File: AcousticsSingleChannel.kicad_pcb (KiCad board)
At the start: 4 copper layers, 25.4 x 25.4 mm, 51 parts, among them J1 Conn_01x04_Pin, J2 Conn_01x04_Pin, J4 Conn_01x09_Pin, U1 OPA1604AIPWR, U2 OPA1604AIPWR, U3 LTC6910-3CTS8#TRPBF, U4 ADS7042IDCUR

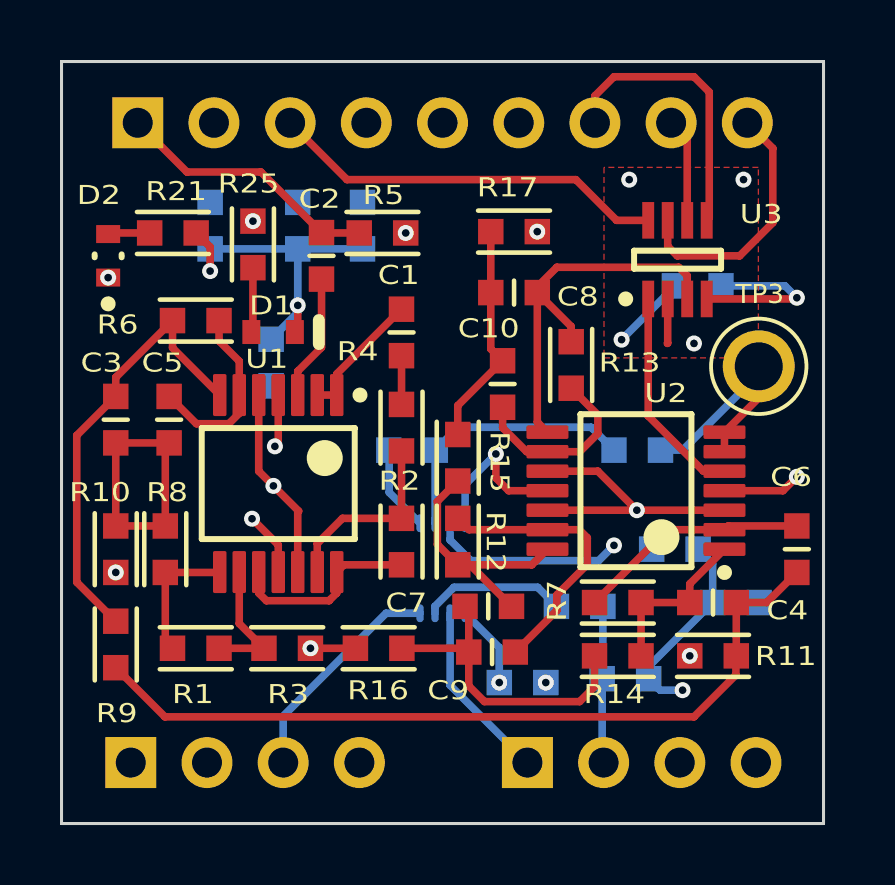
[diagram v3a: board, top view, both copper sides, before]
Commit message: Layer Stackup Updates.
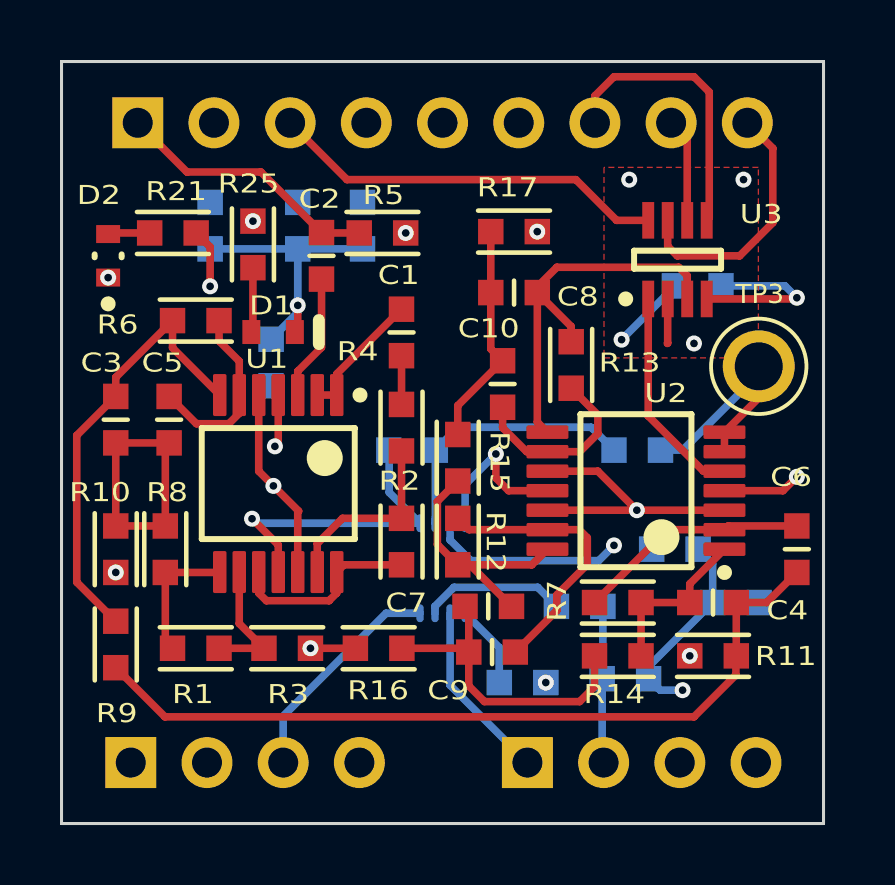
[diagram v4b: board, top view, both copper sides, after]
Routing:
- net GND: track 32.3 -> 38.0 mm
- net +3.3V: vias 5 -> 4
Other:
- board text added: "Single-Channelv1.0"
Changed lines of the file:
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@@
 		(at 144.18306 118.159005 -90)
 		(property "Reference" "C13"
-			(at 0.508 -4.191 0)
+			(at 0.381 1.524 0)
 			(unlocked yes)
 			(layer "B.SilkS")
@@
 		(at 136.69006 102.929165)
 		(property "Reference" "C12"
-			(at 0 2.286 0)
+			(at 0.762 2.286 0)
 			(unlocked yes)
 			(layer "B.SilkS")
@@
 		(at 135.80106 107.491005 180)
 		(property "Reference" "C17"
-			(at -1.016 1.524 0)
+			(at 1.143 -0.254 0)
 			(unlocked yes)
 			(layer "B.SilkS")
@@
 		(tags "Through hole pin header THT 1x04 2.54mm single row")
 		(property "Reference" "J2"
-			(at -2.794 -8.13054 0)
+			(at 0.127 2.70256 0)
 			(layer "B.SilkS")
 			(effects
@@
 		(at 133.76906 102.929165)
 		(property "Reference" "C15"
-			(at 0.254 2.286 0)
+			(at -1.143 0.37084 0)
 			(unlocked yes)
 			(layer "B.SilkS")
@@
 		(at 138.84906 102.929165)
 		(property "Reference" "C14"
-			(at 1.016 2.286 0)
+			(at 3.302 0.11684 0)
 			(unlocked yes)
 			(layer "B.SilkS")
@@
 		(layer "Edge.Cuts")
 	)
+	(gr_text "Single-Channelv1.0"
+		(at 130.34006 105.713005 90)
+		(layer "B.SilkS")
+		(effects
+			(font
+				(size 0.635 0.762)
+				(thickness 0.127)
+			)
+			(justify left bottom mirror)
+		)
+	)
 	(segment
 		(start 136.69006 105.586005)
@@
 	)
 	(segment
+		(start 140.766062 112.849005)
+		(end 135.31706 112.849005)
+		(width 0.254)
+		(layer "B.Cu")
+		(net 1)
+	)
+	(segment
 		(start 138.84906 103.704165)
 		(end 136.69006 103.704165)
@@
 	)
 	(segment
+		(start 135.31706 112.849005)
+		(end 135.16606 112.698005)
+		(width 0.254)
+		(layer "B.Cu")
+		(net 1)
+	)
+	(segment
 		(start 139.73806 110.425005)
 		(end 139.72506 110.412005)
@@
 	)
 	(via
-		(at 143.40806 118.159005)
-		(size 0.5334)
-		(drill 0.254)
-		(layers "F.Cu" "B.Cu")
-		(free yes)
-		(net 21)
-	)
-	(via
 		(at 135.92806 110.285005)
 		(size 0.5334)
@@
 	)
 	(segment
-		(start 133.76906 104.443005)
-		(end 133.76906 103.638005)
+		(start 133.76906 103.638005)
+		(end 133.30406 103.173005)
 		(width 0.254)
 		(layer "F.Cu")
@@
 	)
 	(segment
-		(start 133.76906 103.638005)
-		(end 133.30406 103.173005)
+		(start 133.76906 104.951005)
+		(end 133.76906 103.638005)
 		(width 0.254)
 		(layer "F.Cu")
@@
 	)
 	(via
-		(at 133.76906 104.443005)
+		(at 133.76906 104.951005)
 		(size 0.5334)
 		(drill 0.254)
@@
 	)
 	(segment
-		(start 133.76906 104.443005)
-		(end 139.01906 104.443005)
+		(start 140.28906 103.173005)
+		(end 139.65406 103.808005)
 		(width 0.254)
 		(layer "In1.Cu")
@@
 	)
 	(segment
-		(start 139.01906 104.443005)
-		(end 140.28906 103.173005)
+		(start 139.65406 103.808005)
+		(end 134.91206 103.808005)
 		(width 0.254)
 		(layer "In1.Cu")
@@
 	)
 	(segment
-		(start 131.12492 120.826005)
-		(end 133.76906 118.181865)
+		(start 134.91206 103.808005)
+		(end 133.76906 104.951005)
 		(width 0.254)
-		(layer "In2.Cu")
+		(layer "In1.Cu")
 		(net 34)
 	)
 	(segment
 		(start 133.76906 118.181865)
-		(end 133.76906 104.443005)
+		(end 131.12492 120.826005)
+		(width 0.254)
+		(layer "In2.Cu")
+		(net 34)
+	)
+	(segment
+		(start 133.76906 104.951005)
+		(end 133.76906 118.181865)
 		(width 0.254)
 		(layer "In2.Cu")

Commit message: Layer Stackup Updates.
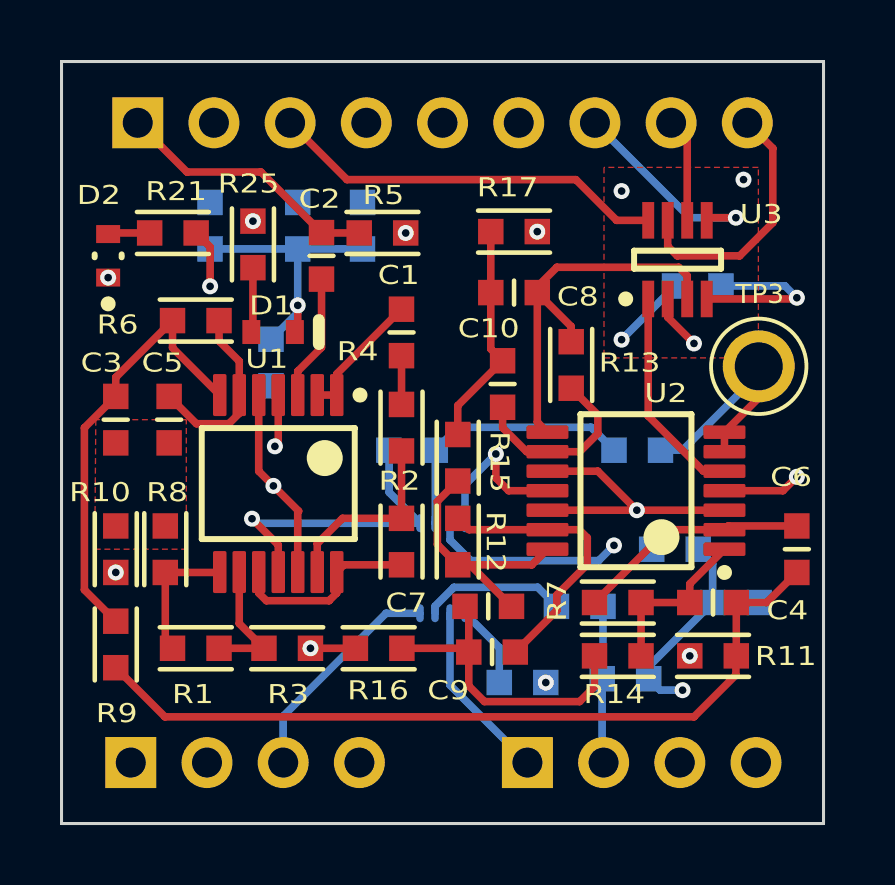
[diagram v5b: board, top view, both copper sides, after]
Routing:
- net /Band Pass Filter/F1_In: track 9.20 -> 0.47 mm
- net /G0_out: track 9.50 -> 7.02 mm, vias 0 -> 1
- added copper zone on F.Cu, net /Band Pass Filter/F1_In
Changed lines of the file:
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@@
-	)
-	(segment
-		(start 149.02206 105.372005)
-		(end 149.02206 106.843005)
-		(width 0.254)
-		(layer "F.Cu")
-		(net 2)
-	)
-	(segment
-		(start 149.02206 106.843005)
-		(end 149.00906 106.856005)
-		(width 0.254)
-		(layer "F.Cu")
-		(net 2)
 	)
 	(segment
@@
 	)
 	(segment
+		(start 149.02206 105.980005)
+		(end 149.89806 106.856005)
+		(width 0.254)
+		(layer "F.Cu")
+		(net 2)
+	)
+	(segment
 		(start 147.99306 112.414005)
 		(end 150.91406 112.414005)
@@
 	)
 	(segment
+		(start 149.02206 105.372005)
+		(end 149.02206 105.980005)
+		(width 0.254)
+		(layer "F.Cu")
+		(net 2)
+	)
+	(segment
 		(start 145.01406 112.414005)
 		(end 147.99306 112.414005)
@@
 	)
 	(via
-		(at 147.73906 101.395005)
+		(at 147.48506 101.776005)
 		(size 0.5334)
 		(drill 0.254)
@@
 	)
 	(segment
-		(start 130.62406 110.171005)
-		(end 130.62406 112.939005)
-		(width 0.254)
-		(layer "F.Cu")
-		(net 13)
-	)
-	(segment
-		(start 130.62406 112.939005)
-		(end 132.27506 112.939005)
-		(width 0.254)
-		(layer "F.Cu")
-		(net 13)
-	)
-	(segment
-		(start 132.27506 110.412005)
-		(end 132.27506 112.939005)
-		(width 0.254)
-		(layer "F.Cu")
-		(net 13)
-	)
-	(segment
 		(start 132.40206 110.171005)
 		(end 132.40206 110.285005)
@@
 	)
 	(segment
-		(start 130.62406 110.171005)
-		(end 132.40206 110.171005)
-		(width 0.254)
-		(layer "F.Cu")
-		(net 13)
-	)
-	(segment
 		(start 132.27506 110.298005)
 		(end 132.40206 110.171005)
@@
 	)
 	(segment
+		(start 129.57806 115.068005)
+		(end 129.57806 109.667005)
+		(width 0.254)
+		(layer "F.Cu")
+		(net 14)
+	)
+	(segment
+		(start 130.62406 116.114005)
+		(end 129.57806 115.068005)
+		(width 0.254)
+		(layer "F.Cu")
+		(net 14)
+	)
+	(segment
 		(start 130.62406 107.986005)
 		(end 132.51606 106.094005)
@@
 	)
 	(segment
-		(start 129.32406 114.814005)
-		(end 129.32406 109.921005)
-		(width 0.254)
-		(layer "F.Cu")
-		(net 14)
-	)
-	(segment
-		(start 129.32406 109.921005)
+		(start 129.57806 109.667005)
 		(end 130.62406 108.621005)
 		(width 0.254)
@@
 	)
 	(segment
-		(start 130.62406 116.114005)
-		(end 129.32406 114.814005)
-		(width 0.254)
-		(layer "F.Cu")
-		(net 14)
-	)
-	(segment
 		(start 130.62406 108.621005)
 		(end 130.62406 107.986005)
@@
 	)
 	(segment
-		(start 150.40606 102.668005)
-		(end 150.40606 98.474005)
+		(start 151.29506 102.665005)
+		(end 150.40906 102.665005)
 		(width 0.254)
 		(layer "F.Cu")
@@
 	)
 	(segment
-		(start 146.59606 98.601005)
-		(end 146.59606 99.500165)
+		(start 150.40906 102.665005)
+		(end 150.32206 102.752005)
 		(width 0.254)
 		(layer "F.Cu")
 		(net 30)
 	)
-	(segment
-		(start 149.89806 97.966005)
-		(end 147.23106 97.966005)
-		(width 0.254)
-		(layer "F.Cu")
+	(via
+		(at 151.29506 102.665005)
+		(size 0.5334)
+		(drill 0.254)
+		(layers "F.Cu" "B.Cu")
+		(free yes)
 		(net 30)
 	)
 	(segment
-		(start 150.40606 98.474005)
-		(end 149.89806 97.966005)
-		(width 0.254)
-		(layer "F.Cu")
+		(start 149.7609 102.665005)
+		(end 151.29506 102.665005)
+		(width 0.254)
+		(layer "B.Cu")
 		(net 30)
 	)
 	(segment
-		(start 150.32206 102.752005)
-		(end 150.40606 102.668005)
-		(width 0.254)
-		(layer "F.Cu")
-		(net 30)
-	)
-	(segment
-		(start 147.23106 97.966005)
-		(end 146.59606 98.601005)
-		(width 0.254)
-		(layer "F.Cu")
+		(start 146.59606 99.500165)
+		(end 149.7609 102.665005)
+		(width 0.254)
+		(layer "B.Cu")
 		(net 30)
 	)
@@
 	)
 	(zone
+		(net 13)
+		(net_name "/Band Pass Filter/F1_In")
+		(layer "F.Cu")
+		(hatch edge 0.5)
+		(priority 4)
+		(connect_pads yes
+			(clearance 0.254)
+		)
+		(min_thickness 0.25)
+		(filled_areas_thickness no)
+		(fill yes
+			(thermal_gap 0.5)
+			(thermal_bridge_width 0.5)
+		)
+		(polygon
+			(pts
+				(xy 129.95906 109.396125) (xy 129.92406 113.714005) (xy 132.97506 113.714005) (xy 132.97506 109.396125)
+			)
+		)
+	)
+	(zone
